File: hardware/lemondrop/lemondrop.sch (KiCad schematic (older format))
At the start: 109 parts, among them P1 GSG-SMA-CONN, P2 GSG-SMA-CONN, P3 CONN_3X2, P4 CONN_3X2, P5 CONN_20X2, P6 CONN_8X2, P7 CONN_6X2, P8 GSG-SMA-CONN, P9 CONN_2, T1 BALUN, T2 BALUN, U1 MAX5864, U2 MAX2837, U3 SI5351C, X1 GSG-XTAL4PIN

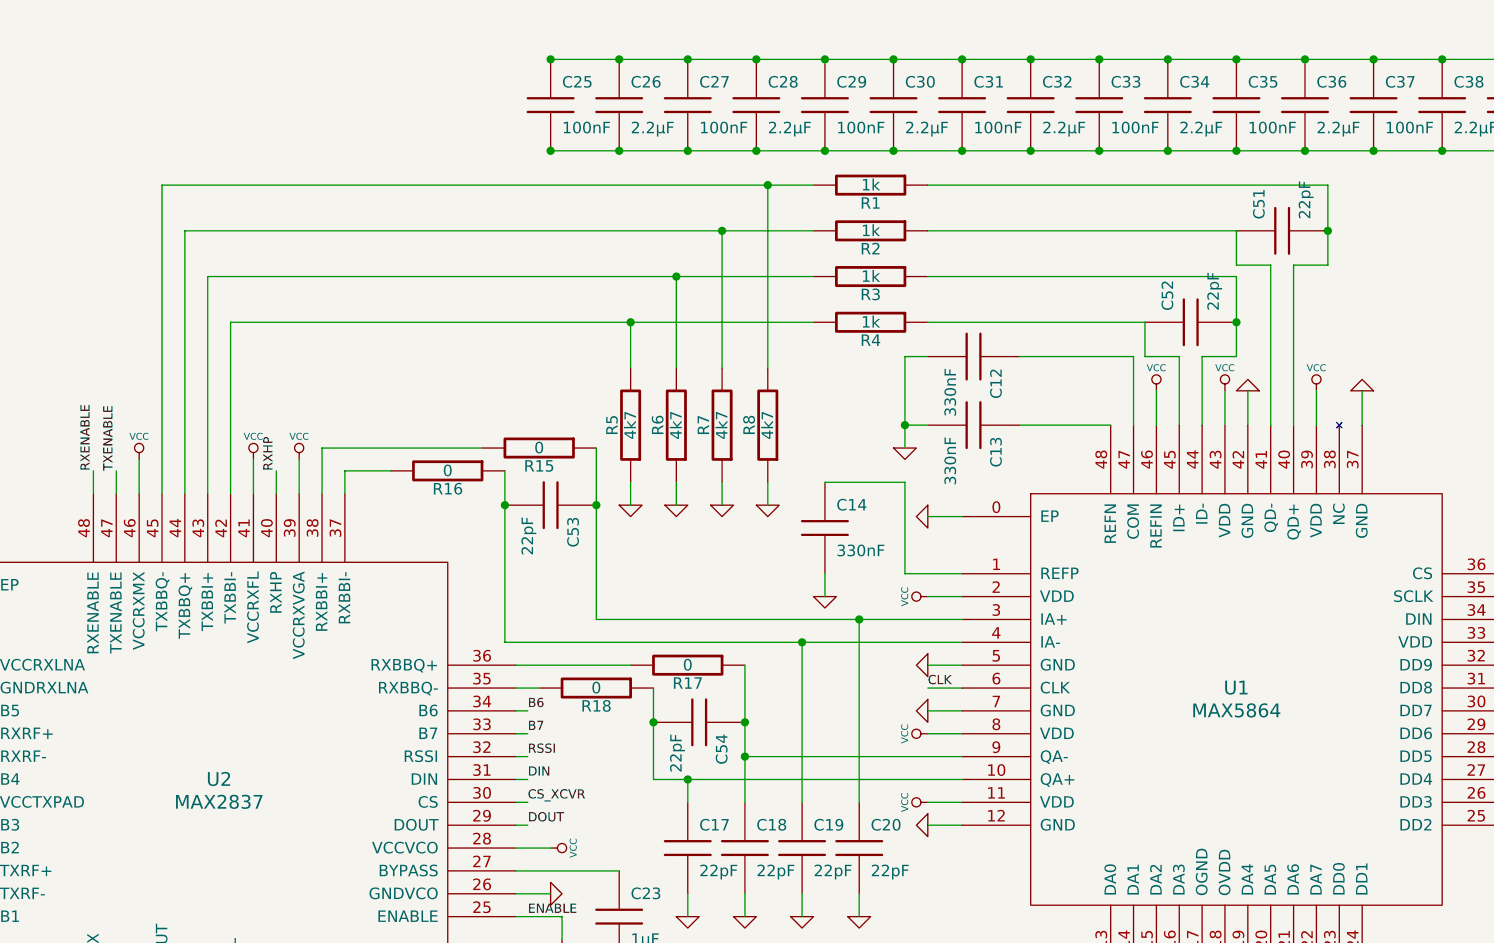
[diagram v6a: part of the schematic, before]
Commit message: corrected C51, C52 positions
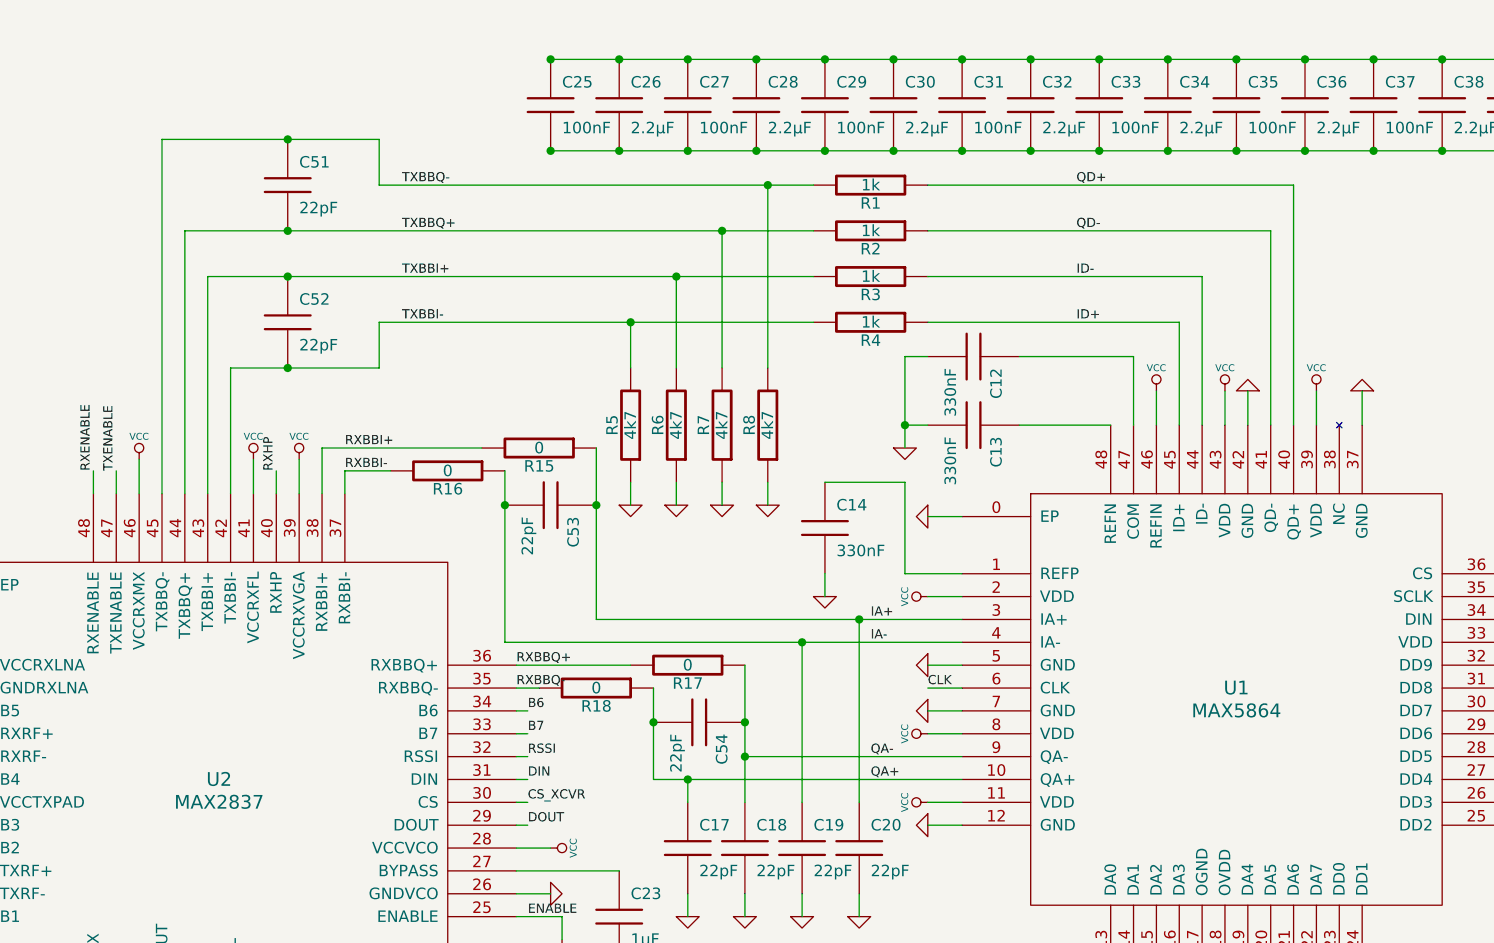
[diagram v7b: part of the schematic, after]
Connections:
- net RXBBQ-: now reaches R18.2, U2.35 (RXBBQ-)
- net RXBBQ+: now reaches R17.2, U2.36 (RXBBQ+)
- net RXBBI-: now reaches R16.2, U2.37 (RXBBI-)
- net RXBBI+: now reaches R15.2, U2.38 (RXBBI+)
- net TXBBI-: now reaches R4.2, R5.2, U2.42 (TXBBI-)
- net TXBBI-: now also C52.2
- net TXBBI+: now reaches R3.2, R6.2, U2.43 (TXBBI+)
- net TXBBI+: now also C52.1
- net TXBBQ+: now reaches R2.2, R7.2, U2.44 (TXBBQ+)
- net TXBBQ+: now also C51.2
- net TXBBQ-: now reaches R1.2, R8.2, U2.45 (TXBBQ-)
- net TXBBQ-: now also C51.1
- net QA+: now reaches C17.1, C54.2, R18.1, U1.10 (QA+)
- net IA+: now reaches C20.1, C53.1, R15.1, U1.3 (IA+)
- net IA-: now reaches C19.1, C53.2, R16.1, U1.4 (IA-)
- net QD+: now reaches R1.1, U1.40 (QD+)
- net QD+: no longer C51.2
- net QD-: now reaches R2.1, U1.41 (QD-)
- net QD-: no longer C51.1
- net ID-: now reaches R3.1, U1.44 (ID-)
- net ID-: no longer C52.2
- net ID+: now reaches R4.1, U1.45 (ID+)
- net ID+: no longer C52.1
- net QA-: now reaches C18.1, C54.1, R17.1, U1.9 (QA-)
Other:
- moved on the sheet: C51, C52
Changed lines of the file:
@@
-EESchema Schematic File Version 2  date Sun 11 Mar 2012 09:59:23 PM MDT
+EESchema Schematic File Version 2  date Sun 11 Mar 2012 10:46:36 PM MDT
 LIBS:power
 LIBS:device
@@
 Comment4 ""
 $EndDescr
+Text Label 9000 1850 0    40   ~ 0
+ID+
+Text Label 9000 1650 0    40   ~ 0
+ID-
+Text Label 9000 1450 0    40   ~ 0
+QD-
+Text Label 9000 1250 0    40   ~ 0
+QD+
+Text Label 8100 3850 0    40   ~ 0
+QA+
+Text Label 8100 3750 0    40   ~ 0
+QA-
+Text Label 8100 3250 0    40   ~ 0
+IA-
+Text Label 8100 3150 0    40   ~ 0
+IA+
+Text Label 6550 3350 0    40   ~ 0
+RXBBQ+
+Text Label 6550 3450 0    40   ~ 0
+RXBBQ-
+Text Label 5800 2500 0    40   ~ 0
+RXBBI-
+Text Label 5800 2400 0    40   ~ 0
+RXBBI+
+Text Label 6050 1850 0    40   ~ 0
+TXBBI-
+Text Label 6050 1650 0    40   ~ 0
+TXBBI+
+Text Label 6050 1450 0    40   ~ 0
+TXBBQ+
+Text Label 6050 1250 0    40   ~ 0
+TXBBQ-
+Connection ~ 5550 1050
+Wire Wire Line
+	5000 1050 5000 2600
+Wire Wire Line
+	5000 1050 5950 1050
+Connection ~ 5550 1450
+Connection ~ 5550 1650
+Wire Wire Line
+	7850 1650 5200 1650
+Connection ~ 5550 2050
+Wire Wire Line
+	5950 2050 5950 1850
+Wire Wire Line
+	5950 2050 5300 2050
+Wire Wire Line
+	8350 1250 9950 1250
+Wire Wire Line
+	9950 1250 9950 2300
+Wire Wire Line
+	8350 1650 9550 1650
+Wire Wire Line
+	9550 1650 9550 2300
 Connection ~ 600  7350
 Wire Wire Line
@@
 Wire Wire Line
 	3650 4350 3650 4850
-Wire Wire Line
-	8350 1450 9700 1450
-Connection ~ 10100 1450
-Wire Wire Line
-	9950 2300 9950 1600
-Wire Wire Line
-	9950 1600 10100 1600
-Wire Wire Line
-	10100 1600 10100 1250
-Wire Wire Line
-	8350 1850 9300 1850
-Connection ~ 9700 1850
-Wire Wire Line
-	8350 1650 9700 1650
-Wire Wire Line
-	9700 1650 9700 2000
 Wire Wire Line
 	6900 2400 6900 3150
@@
 Connection ~ 7050 1850
 Wire Wire Line
-	7050 2050 7050 1850
+	7050 1850 7050 2050
 Connection ~ 7450 1450
 Wire Wire Line
-	7450 2050 7450 1450
-Wire Wire Line
-	5300 2600 5300 1850
-Wire Wire Line
-	5300 1850 7850 1850
+	7450 1450 7450 2050
 Wire Wire Line
 	5100 2600 5100 1450
-Wire Wire Line
-	5100 1450 7850 1450
 Wire Wire Line
 	5700 2600 5700 2400
@@
 	5800 2500 5800 2600
 Wire Wire Line
-	5000 2600 5000 1250
-Wire Wire Line
-	5000 1250 7850 1250
-Wire Wire Line
-	7850 1650 5200 1650
-Wire Wire Line
 	5200 1650 5200 2600
 Wire Wire Line
-	7650 2050 7650 1250
+	7650 1250 7650 2050
 Connection ~ 7650 1250
 Wire Wire Line
-	7250 2050 7250 1650
+	7250 1650 7250 2050
 Connection ~ 7250 1650
 Wire Wire Line
@@
 	6500 3250 6500 2500
 Wire Wire Line
-	9550 2300 9550 2000
-Wire Wire Line
-	9550 2000 9700 2000
-Wire Wire Line
-	9450 2300 9450 2000
-Wire Wire Line
-	9450 2000 9300 2000
-Wire Wire Line
-	9300 2000 9300 1850
-Wire Wire Line
-	10100 1250 8350 1250
-Wire Wire Line
-	9850 2300 9850 1600
-Wire Wire Line
-	9850 1600 9700 1600
-Wire Wire Line
-	9700 1600 9700 1450
-Wire Wire Line
 	2700 3450 2600 3450
 Wire Wire Line
@@
 Wire Wire Line
 	3650 1600 3750 1600
+Wire Wire Line
+	8350 1850 9450 1850
+Wire Wire Line
+	9450 1850 9450 2300
+Wire Wire Line
+	8350 1450 9850 1450
+Wire Wire Line
+	9850 1450 9850 2300
+Wire Wire Line
+	5300 2050 5300 2600
+Wire Wire Line
+	5950 1850 7850 1850
+Wire Wire Line
+	5100 1450 7850 1450
+Wire Wire Line
+	7850 1250 5950 1250
+Wire Wire Line
+	5950 1250 5950 1050
 $Comp
 L GND #PWR01
@@
 L C C51
 U 1 1 4F5D697F
-P 9900 1450
-F 0 "C51" H 9950 1550 50  0000 L CNN
-F 1 "22pF" H 9950 1350 50  0000 L CNN
-	1    9900 1450
-	0    -1   -1   0
+P 5550 1250
+F 0 "C51" H 5600 1350 50  0000 L CNN
+F 1 "22pF" H 5600 1150 50  0000 L CNN
+	1    5550 1250
+	1    0    0    -1
 $EndComp
 $Comp
 L C C52
 U 1 1 4F5D6938
-P 9500 1850
-F 0 "C52" H 9550 1950 50  0000 L CNN
-F 1 "22pF" H 9550 1750 50  0000 L CNN
-	1    9500 1850
-	0    -1   -1   0
-$EndComp
-$Comp
+P 5550 1850
+F 0 "C52" H 5600 1950 50  0000 L CNN
+F 1 "22pF" H 5600 1750 50  0000 L CNN
+	1    5550 1850
+	1    0    0    -1
+$EndComp
+$Comp

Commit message: schematic cleanup
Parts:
- P1: value GSG-SMA-CONN -> RX_SMA
- P2: value GSG-SMA-CONN -> TX_SMA
- P3: value CONN_3X2 -> SPI
- P4: value CONN_3X2 -> POWER
- P5: value CONN_20X2 -> ADC/DAC
- P6: value CONN_8X2 -> XCVR_CTL
- P7: value CONN_6X2 -> CLOCK_CTL
- T1: value BALUN -> RX_BALUN
- T2: value BALUN -> TX_BALUN
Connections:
- net CPOUT+: now reaches C40.2, R9.1, U2.23 (CPOUT+)
- net CPOUT-: now reaches C40.1, R10.1, U2.24 (CPOUT-)
- net REFP: now reaches C14.1, U1.1 (REFP)
- net COM: now reaches C12.1, U1.47 (COM)
- net REFN: now reaches C13.1, U1.48 (REFN)
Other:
- moved on the sheet: C1, C10, C11, C12, C13, C14, C15, C16, C17, C18, C19, C2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
